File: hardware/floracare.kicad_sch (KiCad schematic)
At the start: 23 parts, among them J2 Conn_01x04_Socket, J4 Conn_01x04_Socket, J5 Conn_01x14_Socket, J6 Conn_01x05_Socket, SW1 SW_Push, SW2 SW_Push, U1 AMS1117-3.3, U2 ESP32-S3-WROOM-1

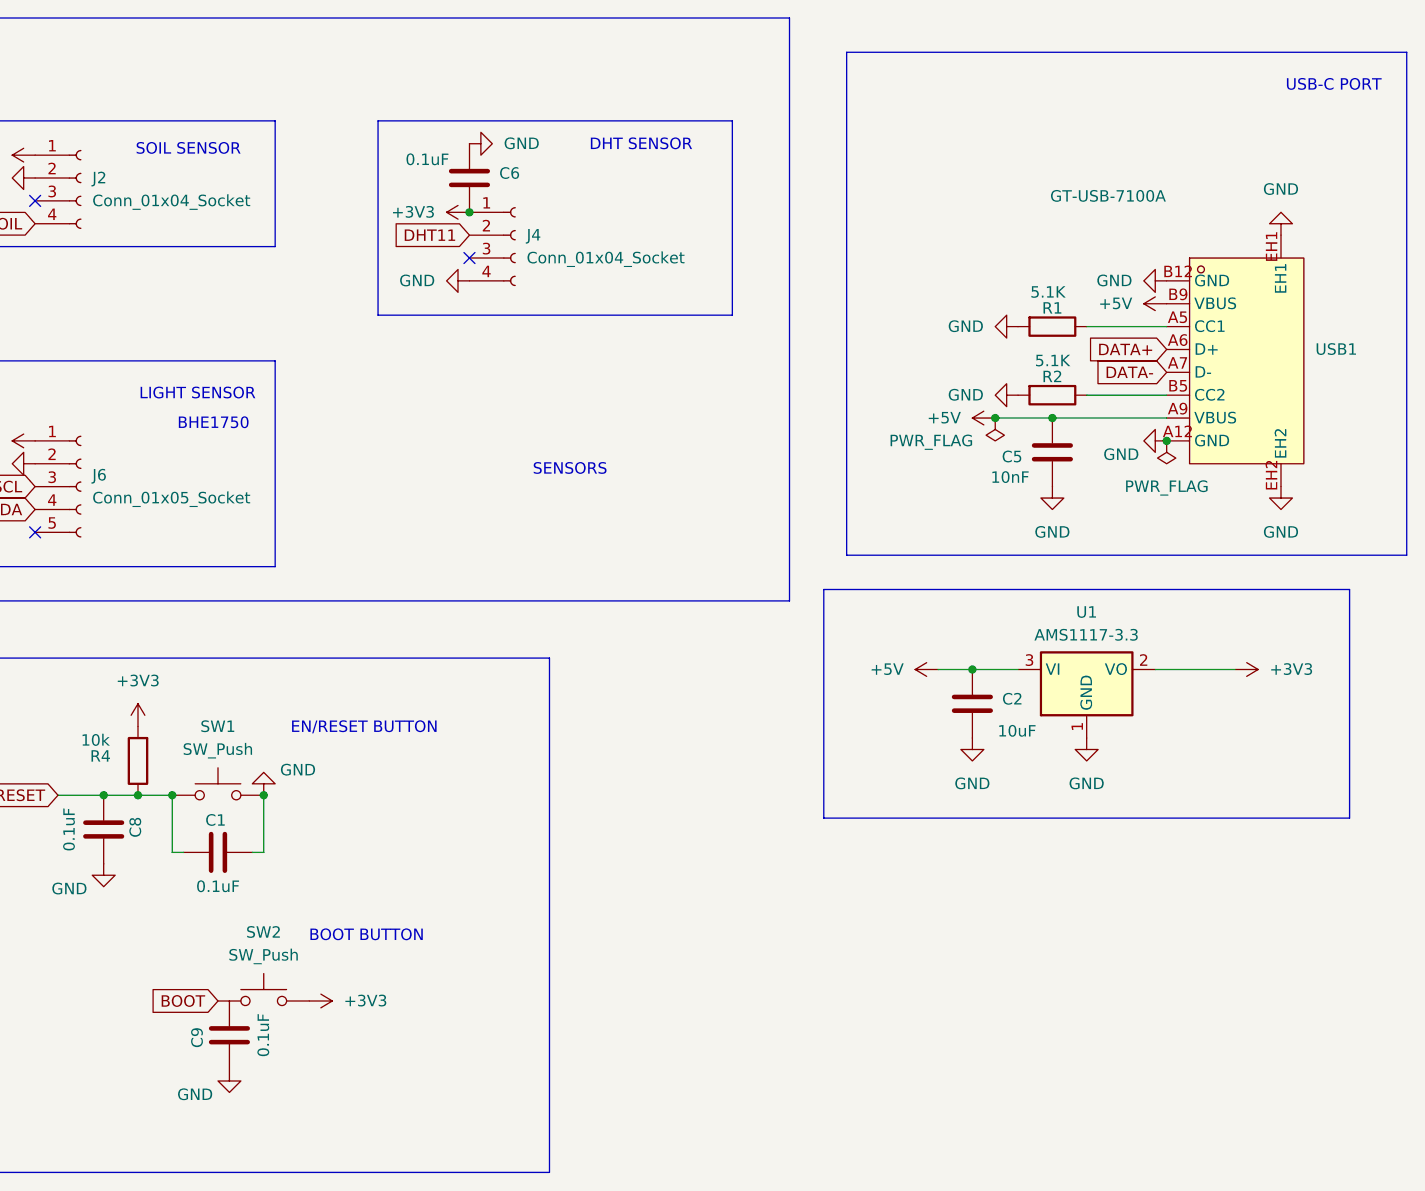
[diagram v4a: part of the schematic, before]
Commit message: Finishing PCB , [USBC NOT STABLE WITH DRC]
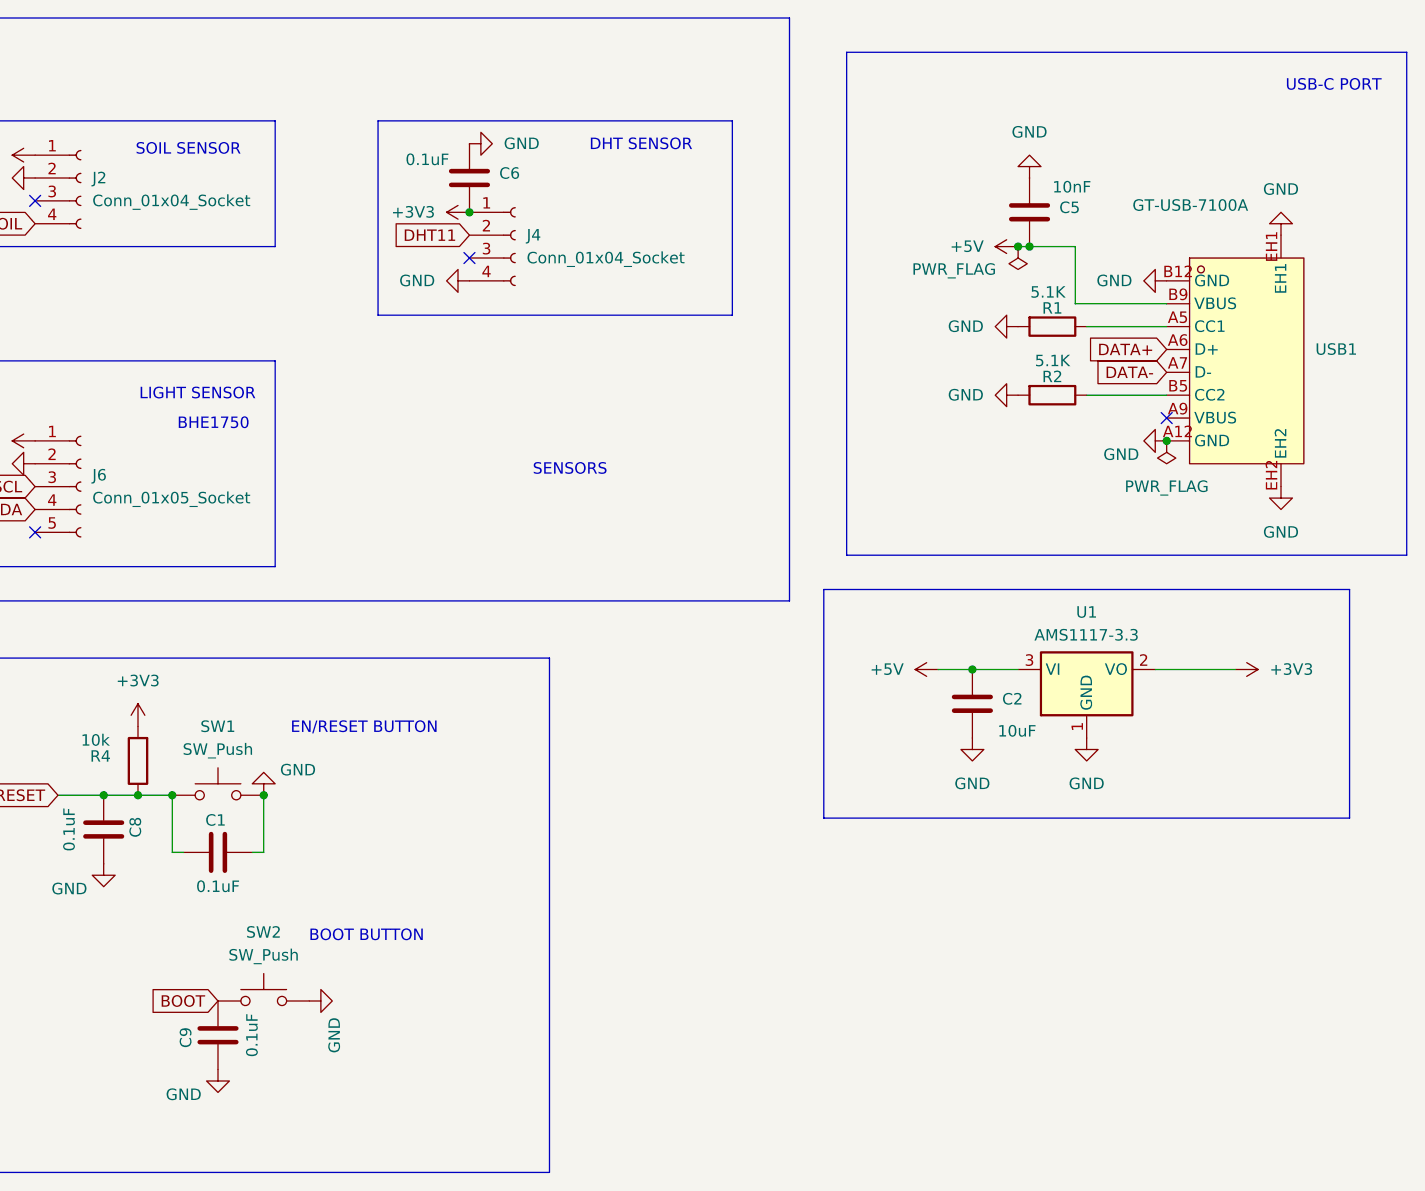
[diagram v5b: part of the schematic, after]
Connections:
- net +3V3: no longer SW2.2
- net +5V: no longer USB1.A9 (VBUS)
- net BOOT: now also C9.2
- net GND: now also SW2.2
- no-connect marks 32 -> 33
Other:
- moved on the sheet: C5, C9

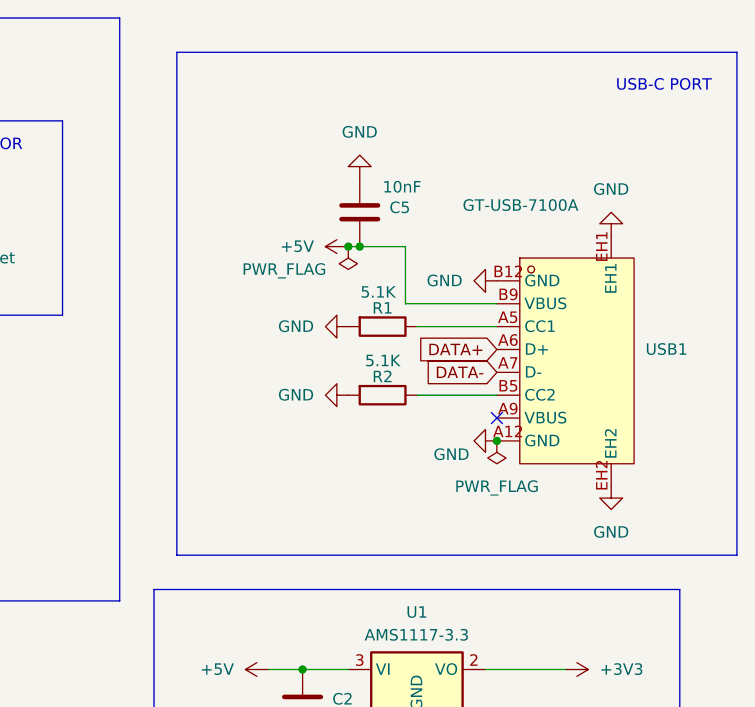
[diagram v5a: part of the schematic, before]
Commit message: Finishing USB-C Routing & PCB [DRC STABLE]
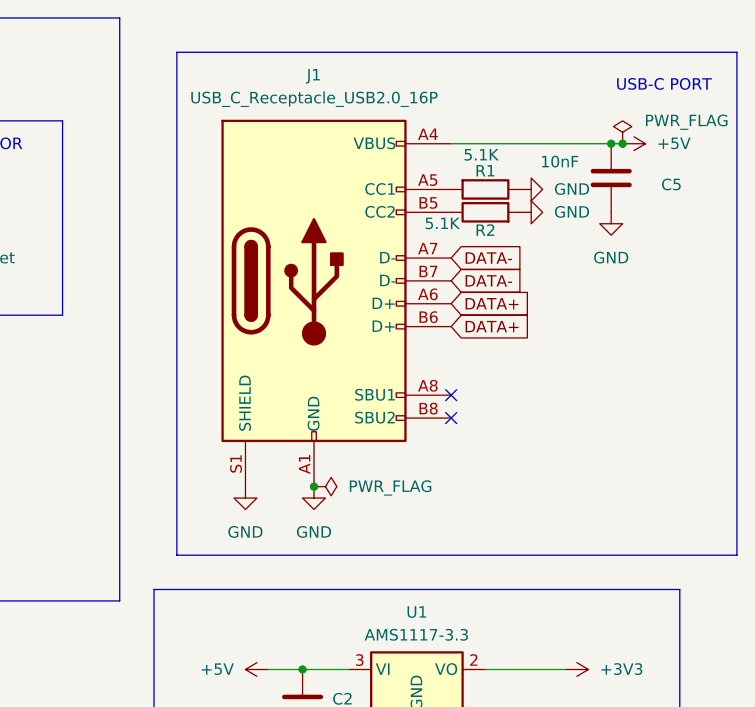
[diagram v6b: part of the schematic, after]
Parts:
- removed USB1: GT-USB-7100A, easyeda2kicad:USB-C-SMD_GT-USB-7100A, symbol usbeasy:GT-USB-7100A
- added J1: USB_C_Receptacle_USB2.0_16P, Connector_USB:USB_C_Receptacle_HCTL_HC-TYPE-C-16P-01A, symbol Connector:USB_C_Receptacle_USB2.0_16P
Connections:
- net +5V: now also J1.A4 (VBUS), J1.A9 (VBUS), J1.B4 (VBUS), J1.B9 (VBUS)
- net DATA+: now also J1.A6 (D+), J1.B6 (D+)
- net DATA-: now also J1.A7 (D-), J1.B7 (D-)
- net GND: now also R1.1, J1.A1 (GND), J1.A12 (GND), J1.B1 (GND), J1.B12 (GND), J1.S1 (SHIELD); no longer R1.2
- net at R2.1: now also J1.B5 (CC2)
- new net: J1.A5 (CC1), R1.2
- no-connect marks 33 -> 34
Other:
- moved on the sheet: C5
